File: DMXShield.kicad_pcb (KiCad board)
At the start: 2 copper layers, 41 x 60.5 mm, 42 parts, among them CN12 CONN_PWR12V, IC1 ATMEGA328P-A, K1 XLR3, M1 DS2431, Q1 Q_NMOS_GDS, Q2 Q_NMOS_GDS, Q3 Q_NMOS_GDS, U1 6N136, U13 CONN_02X20, U14 CONN_02X20, U2 6N136, U3 6N136

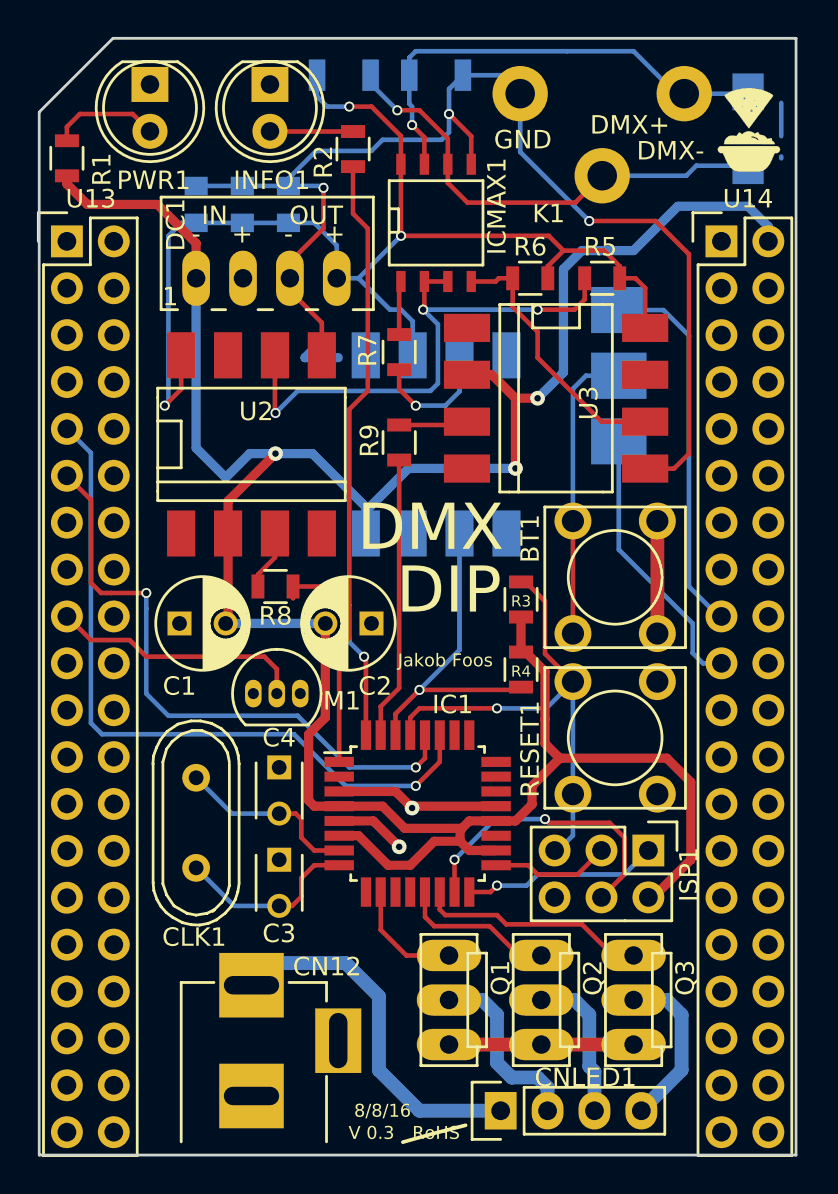
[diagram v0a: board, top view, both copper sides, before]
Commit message: First layout for V1.0
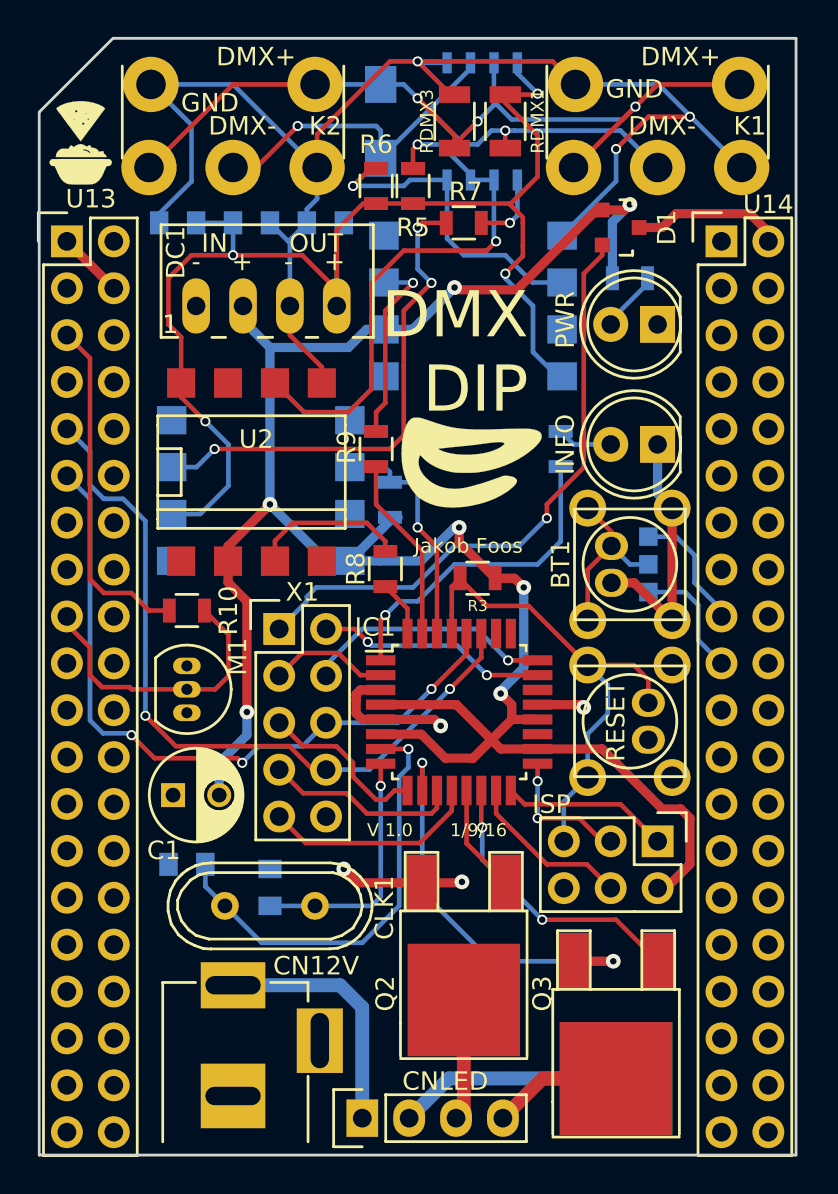
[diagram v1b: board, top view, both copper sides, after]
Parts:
- removed C2: 10u, Capacitors_ThroughHole:C_Radial_D5_L11_P2.5
- removed CN12: CONN_PWR12V, MyLib1:BARREL_JACK_Silk
- removed RESET1: SW_PUSH, MyLib1:SWITCH_SMALL
- added CN12V: CONN_PWR12V, MyLib1:BARREL_JACK_Silk, F.Cu at (60.5, 97.0)
- added D1: D_Schottky_x2_ACom_KKA, TO_SOT_Packages_SMD:SOT-23, F.Cu at (81.5, 49.8)
- added G***: LOGO, MyLib1:Erebos3D-Logo-Smaller, B.Cu at (74.8, 76.0)
- added G***: LOGO, MyLib1:E-Logo2, F.Cu at (73.2, 62.5)
- added K2: XLR3, MyLib1:XLR_Angled_DoubleWay, F.Cu at (60.5, 42.0)
- added R10: 4K7, Resistors_SMD:R_0805, F.Cu at (58.0, 70.5)
- added RESET: SW_PUSH, MyLib1:Switch_Plus_Connector, F.Cu at (82.0, 76.5)
- added X1: CONN_02X05, Pin_Headers:Pin_Header_Straight_2x05, F.Cu at (63.0, 71.5)
- BT1: footprint MyLib1:SWITCH_SMALL -> MyLib1:Switch_Plus_Connector
- C3, C4: footprint Capacitors_ThroughHole:C_Disc_D3_P2.5 -> Capacitors_SMD:C_0805; moved to B.Cu
- IC2: renamed from ICMAX1; moved to B.Cu
- K1: footprint MyLib1:XLR_Angled_Silk -> MyLib1:XLR_Angled_DoubleWay
- Q1: footprint MyLib1:IRLU_THT_Upstanding -> TO_SOT_Packages_SMD:TO-252-2Lead; moved to B.Cu
- Q2, Q3: footprint MyLib1:IRLU_THT_Upstanding -> TO_SOT_Packages_SMD:TO-252-2Lead
- R1, R2, R4: moved to B.Cu
- RDMX1, RDMX3: moved to F.Cu
- SJP1: footprint MyLib1:Solder_Jumper_3 -> MyLib1:Solder_Jumper_3_SMALL
- U1, U2: footprint MyLib1:DIP-8_SMD -> MyLib1:DIP-8_SMD_Smaller
- U3: footprint MyLib1:DIP-8_SMD -> MyLib1:DIP-8_SMD_Smaller; moved to B.Cu
- moved G*** 36.2 mm to (52.3, 45.2)
- moved R1 31.2 mm to (82.0, 52.5), turned to 180 degrees
- moved PWR 30.4 mm to (83.5, 55.0), turned to 180 degrees
- moved INFO 28.7 mm to (83.5, 61.5), turned to 180 degrees
- moved RDMX2 19.9 mm to (68.5, 44.0)
- moved R2 19.8 mm to (78.2, 61.8)
- moved R4 11.6 mm to (69.0, 64.5), turned to 270 degrees
- moved R5 11.4 mm to (70.2, 47.5), turned to 270 degrees
- moved SJP1 11.4 mm to (83.0, 67.2)
- moved U1 9.82 mm to (62.0, 64.0), turned to 90 degrees
- moved R6 9.73 mm to (68.2, 47.5), turned to 270 degrees
- moved C1 9.31 mm to (57.2, 80.5)
- moved Q1 9.29 mm to (81.2, 89.5), turned to 0 degrees
- moved RDMX1 9.10 mm to (75.2, 44.0), turned to 90 degrees
- moved R7 7.83 mm to (73.0, 49.5), turned to 0 degrees
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- renumbered CNLED1 to CNLED, INFO1 to INFO, ISP1 to ISP, PWR1 to PWR
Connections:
- DC1 pad 1: 5V -> GND
- DC1 pad 2: GND -> 5V
- IC1 pad 11: Net-(IC1-Pad11) -> X_IO2
- IC1 pad 12: Net-(IC1-Pad12) -> X_IO3
- IC1 pad 2: Net-(IC1-Pad2) -> X_IO0
- IC1 pad 23: Net-(IC1-Pad23) -> X_ADC0
- IC1 pad 24: Net-(IC1-Pad24) -> X_ADC1
- IC1 pad 9: Net-(IC1-Pad9) -> X_IO1
- U13 pad 3: 5V -> Net-(U13-Pad3)
- U14 pad 2: 5V -> Net-(D1-Pad3)
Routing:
- net X_5V: track 0.00 -> 33.2 mm, vias 0 -> 1
- net 5V: track 149.2 -> 120.5 mm, vias 3 -> 7
- net Net-(R7-Pad1): track 6.97 -> 27.1 mm, vias 1 -> 3
- net 3V3: track 0.00 -> 18.7 mm
- net Net-(ICMAX1-Pad7): track 27.3 -> 44.9 mm, vias 1 -> 3
- net INFO: track 33.2 -> 17.8 mm, vias 0 -> 1
- net Net-(C4-Pad2): track 9.97 -> 24.0 mm, vias 0 -> 1
- net X_ADC1: track 0.00 -> 13.8 mm, vias 0 -> 1
- net P4: track 20.4 -> 6.84 mm
- net X_ADC0: track 0.00 -> 13.1 mm, vias 0 -> 2
- net Net-(IC1-Pad10): track 6.32 -> 18.3 mm, vias 0 -> 1
- net X_IO3: track 0.00 -> 11.8 mm
- net GND_EXT: track 67.2 -> 78.4 mm
- net X_IO2: track 0.00 -> 10.6 mm
- net X_IO1: track 0.00 -> 9.32 mm
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- added copper zone on F.Cu, net (none)
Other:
- board text added: "1/9/16"
- board text added: "DMX DIP"
- board text added: "For more information, please visit"
- board text added: "JP1 and JP2 are not on the board, thus the isolation is not optional. Ideas: Better name?"
- board text added: "P4"
- board text added: "P6"
- board text added: "The plane on Front is for a stronger color of the pcb."
- board text added: "V 1.0"
- board text added: "https://github.com/Erebos3D/DMX-Dip"
- board text removed: "8/8/16"
- board text removed: "Add the resistor for the EEPROM and re-wire the DC/DC converter!"
- board text removed: "DIP"
- board text removed: "DMX"
- board text removed: "RoHS"
- board text removed: "V 0.3"

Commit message: Added decoupling capacitors
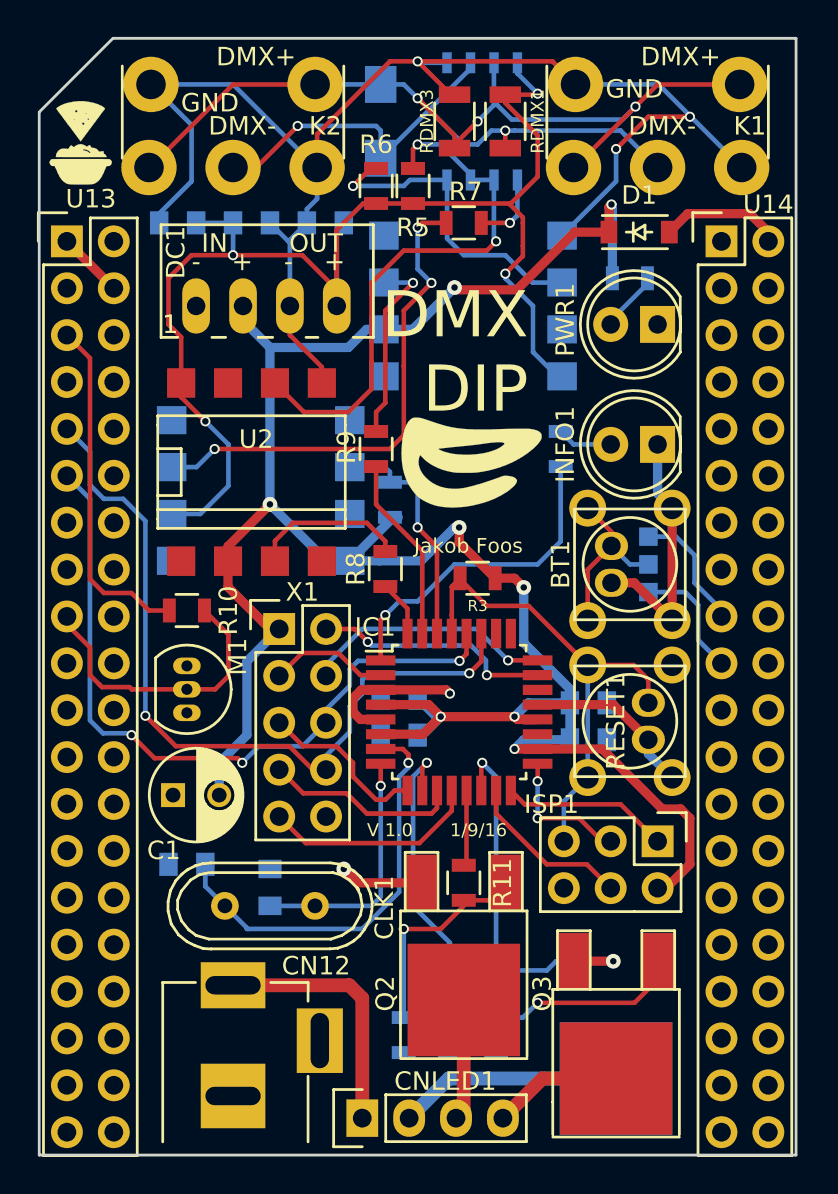
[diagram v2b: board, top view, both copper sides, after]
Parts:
- added C10: 100n, Capacitors_SMD:C_0805, B.Cu at (79.8, 77.5)
- added C11: 100n, Capacitors_SMD:C_0805, B.Cu at (79.8, 75.5)
- added C8: 100n, Capacitors_SMD:C_0805, B.Cu at (69.5, 75.2)
- added C9: 100n, Capacitors_SMD:C_0805, B.Cu at (69.5, 77.2)
- added R11: 100, Resistors_SMD:R_0805, F.Cu at (73.0, 85.2)
- added R12: 100, Resistors_SMD:R_0805, B.Cu at (74.8, 90.0)
- added R13: 100, Resistors_SMD:R_0805, B.Cu at (72.2, 90.0)
- added R14: 4K7, Resistors_SMD:R_0805, B.Cu at (72.2, 93.5)
- added R15: 4K7, Resistors_SMD:R_0805, B.Cu at (74.8, 93.5)
- added R16: 4K7, Resistors_SMD:R_0805, B.Cu at (69.8, 93.5)
- D1: value D_Schottky_x2_ACom_KKA -> D_Schottky; footprint TO_SOT_Packages_SMD:SOT-23 -> Diodes_SMD:SOD-123
- moved D1 1.03 mm to (82.5, 50.0), turned to 0 degrees
- renumbered CN12V to CN12, CNLED to CNLED1, IC2 to ICMAX1, INFO to INFO1, ISP to ISP1, PWR to PWR1, RESET to RESET1
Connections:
- D1 pad 2: X_5V -> Net-(D1-Pad2)
- Q1 pad 1: Net-(IC1-Pad10) -> Net-(Q1-Pad1)
- Q2 pad 1: Net-(IC1-Pad13) -> Net-(Q2-Pad1)
- Q3 pad 1: Net-(IC1-Pad14) -> Net-(Q3-Pad1)
- U14 pad 2: Net-(D1-Pad3) -> Net-(D1-Pad2)
- X1 pad 1: X_5V -> 5V
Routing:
- net X_5V: track 33.2 -> 0.00 mm, vias 1 -> 0
- net Net-(Q3-Pad1): track 0.00 -> 13.0 mm, vias 0 -> 1
- net Net-(Q2-Pad1): track 0.00 -> 12.0 mm, vias 0 -> 1
- net Net-(Q1-Pad1): track 0.00 -> 8.91 mm
- net Net-(D1-Pad3): track 8.23 -> 0.00 mm
- net Net-(D1-Pad2): track 0.00 -> 6.69 mm
- net 5V: track 120.5 -> 127.0 mm, vias 7 -> 8
- net Net-(IC1-Pad10): track 18.3 -> 13.0 mm
- net GND: track 36.4 -> 41.6 mm, vias 5 -> 3
- net Net-(IC1-Pad14): track 15.6 -> 12.1 mm, vias 2 -> 1
- net TWI1-SDA: track 41.1 -> 43.0 mm
- net Net-(IC1-Pad13): track 5.88 -> 4.11 mm
- net Net-(C4-Pad2): track 24.0 -> 22.8 mm
- net TWI1-SCK: track 38.8 -> 39.8 mm
- net RESET: track 27.9 -> 27.0 mm
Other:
- net class PWR: via_dia 0.8 -> 0.55
